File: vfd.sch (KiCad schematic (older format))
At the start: 28 parts, among them Q1 AO3400A, Q13 TO-252, Q14 CJT04N15, Q2 AO3400A, T1 Wuerth 760390013, T2 Wuerth 760390013, T3 Wuerth 760390013, U1 SN74AVC8T245PW, U4 MN12864K

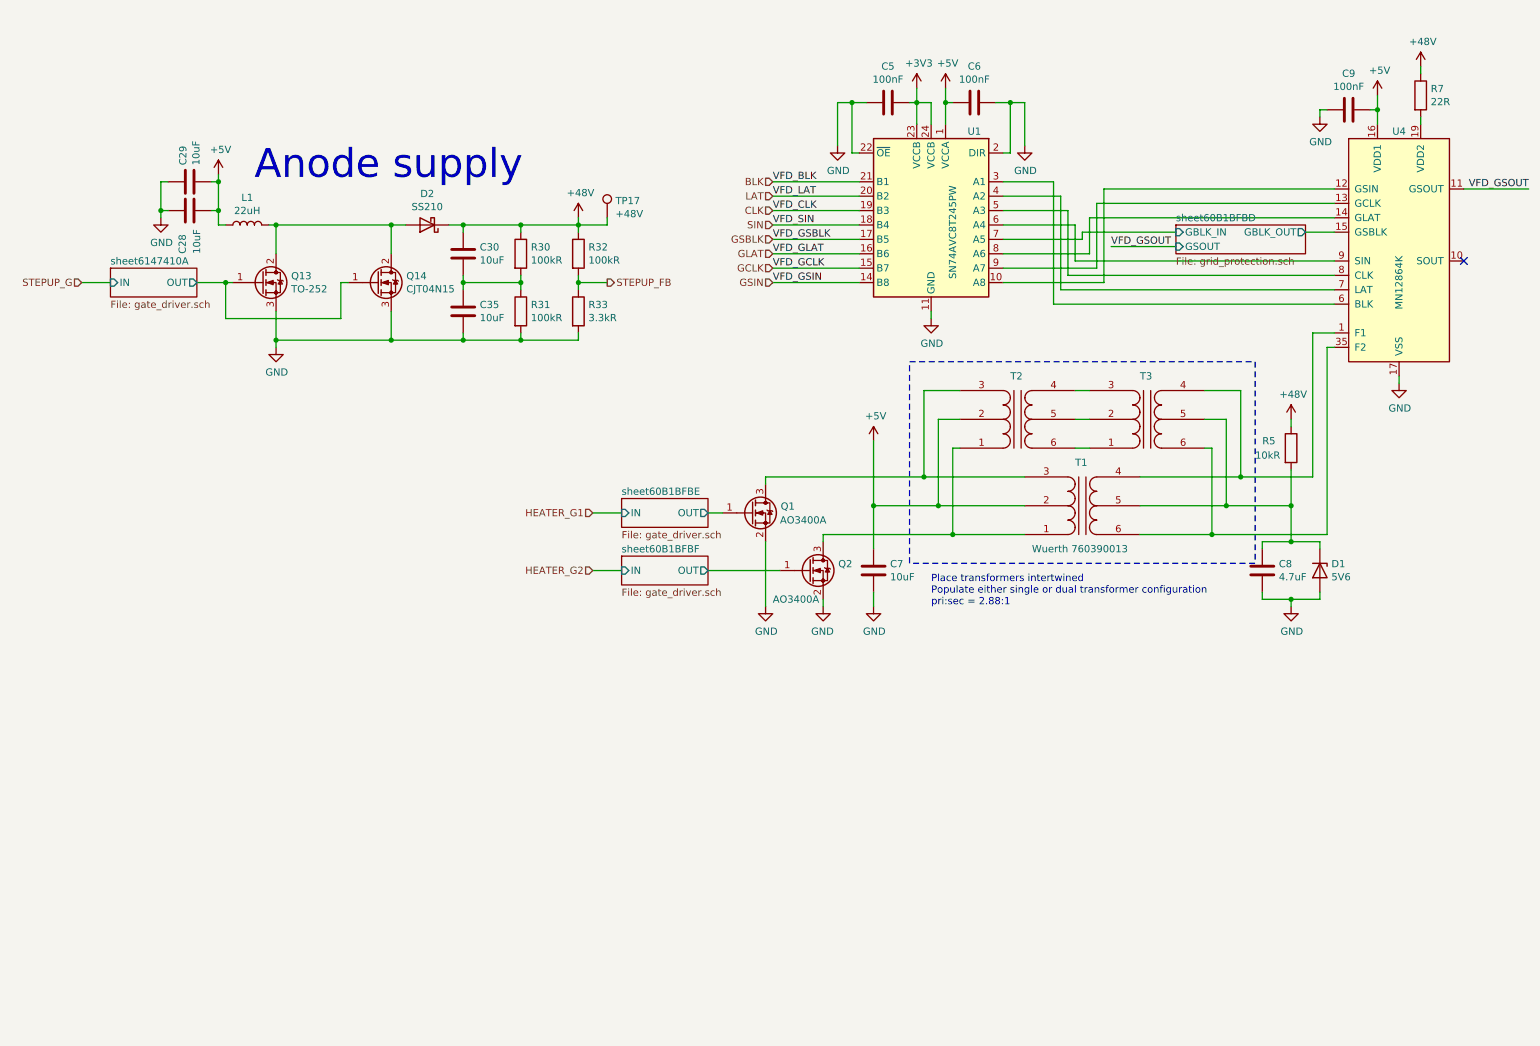
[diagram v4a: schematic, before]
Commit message: Add additional VFD VDD2 bulk capacitance
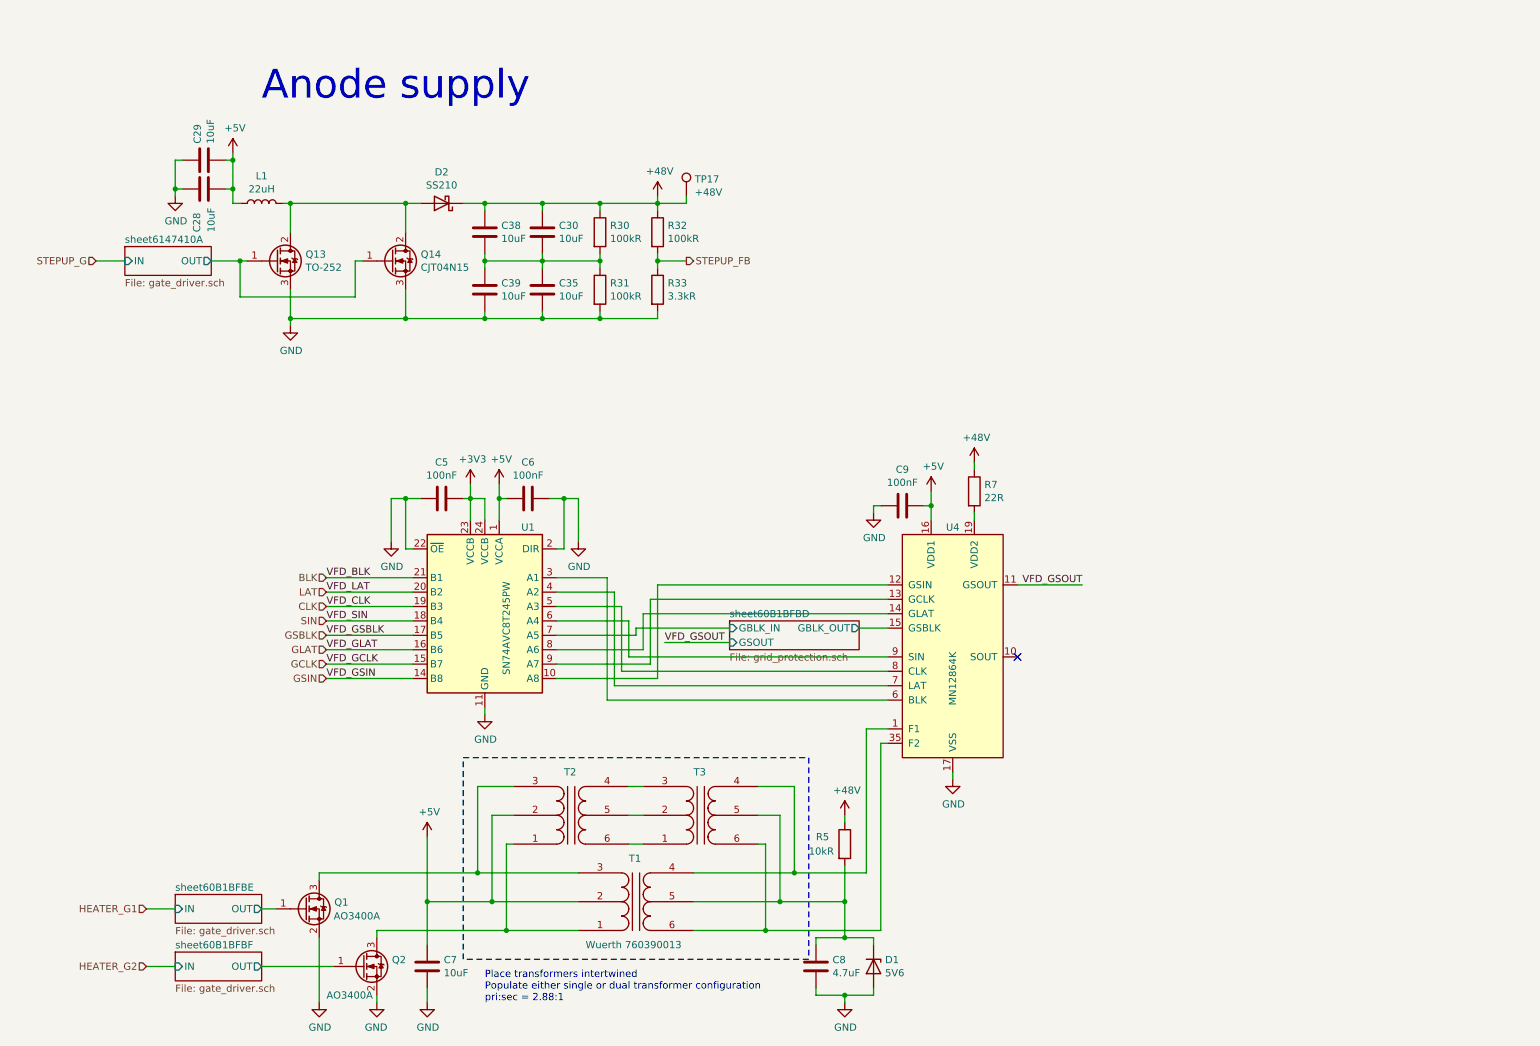
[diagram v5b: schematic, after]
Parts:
- added C38, C39: 10uF, Capacitor_SMD:C_1206_3216Metric, symbol Device:C
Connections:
- net +48V: now also C38.1
- net GND: now also C39.2
- net at C30.2, C35.1, R30.2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: now also C38.2, C39.1
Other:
- moved on the sheet: C28, C29, C30, C35, C5, C6, C7, C8, C9, D1, D2, L1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

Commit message: Add more VFD VDD2 bulk capacitance
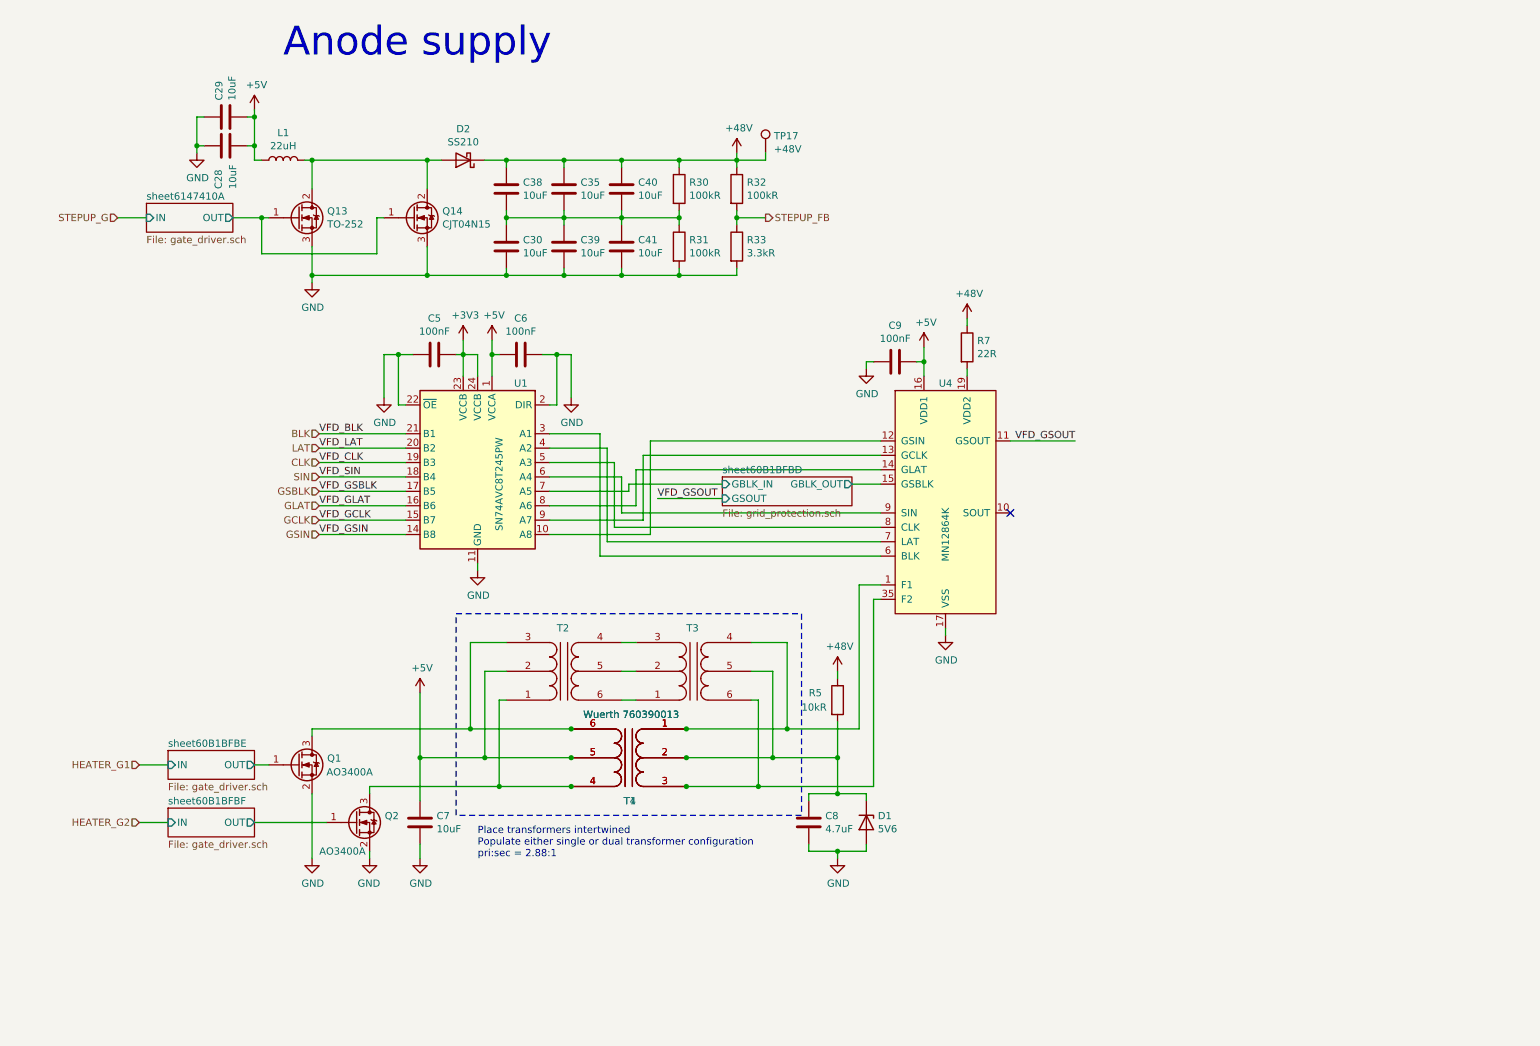
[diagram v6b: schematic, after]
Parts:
- added C40, C41: 10uF, Capacitor_SMD:C_0805_2012Metric, symbol Device:C
- added T4: Wuerth 760390013, Transformer_Würth:Transformer_Würth_12.60x8.30_6P, symbol Transformer_Isolation:Transformer_SP_SS
- C30, C35, C38, C39: footprint Capacitor_SMD:C_1206_3216Metric -> Capacitor_SMD:C_0805_2012Metric; LCSC C13585 -> C440198
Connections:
- net +48V: now also C35.1, C40.1; no longer C30.1
- net +5V: now also T1.5, T4.5; no longer T1.2
- net GND: now also C30.2, C41.2; no longer C35.2
- net at C38.2, C39.1, R30.2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: now also C30.1, C35.2, C40.2, C41.1; no longer C30.2, C35.1
- net at T3.4, U4.1 (F1), U4.2 (F1)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: now also T1.1, T4.1; no longer T1.4
- net at T3.6, U4.35 (F2), U4.36 (F1)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: now also T1.3, T4.3; no longer T1.6
- net at Q2.3 (D), T2.1: now also T1.4, T4.4; no longer T1.1
- net at Q1.3 (D), T2.3: now also T1.6, T4.6; no longer T1.3
- net at C8.1, D1.1 (K), R5.2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: now also T1.2, T4.2; no longer T1.5
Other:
- moved on the sheet: C28, C29, C38, C5, C6, C7, C8, C9, D1, D2, L1, Q1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

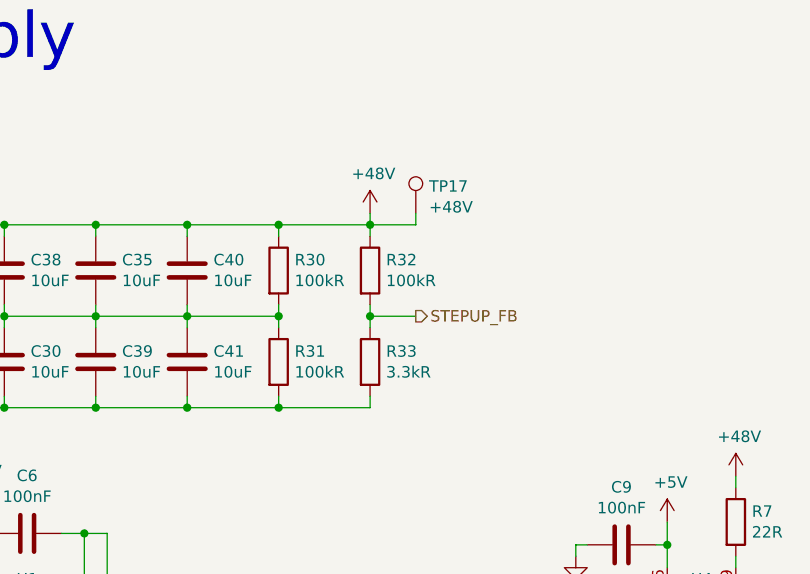
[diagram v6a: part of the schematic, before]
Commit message: Add more VFD VDD2 bypassing
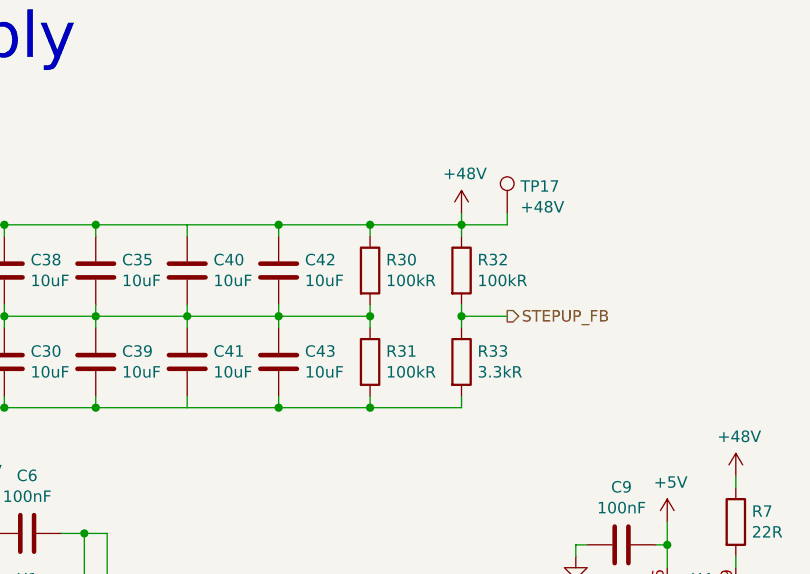
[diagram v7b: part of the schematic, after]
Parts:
- added C42, C43: 10uF, Capacitor_SMD:C_0805_2012Metric, symbol Device:C
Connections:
- net +48V: now also C42.1
- net GND: now also C43.2
- net at C30.1, C35.2, C38.2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: now also C42.2, C43.1
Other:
- moved on the sheet: R30, R31, R32, R33, TP17
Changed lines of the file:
@@
 L Device:R R?
 U 1 1 60D5616D
-P 5550 2150
+P 5950 2150
 AR Path="/60B03476/60D3C691/60D5616D" Ref="R?"  Part="1"
 AR Path="/60B03476/60D5616D" Ref="R33"  Part="1"
-F 0 "R33" H 5620 2196 50  0000 L CNN
-F 1 "3.3kR" H 5620 2105 50  0000 L CNN
-F 2 "Resistor_SMD:R_0402_1005Metric" V 5480 2150 50  0001 C CNN
-F 3 "https://datasheet.lcsc.com/szlcsc/Uniroyal-Elec-0402WGF5101TCE_C25905.pdf" H 5550 2150 50  0001 C CNN
-F 4 "C25890" H 5550 2150 50  0001 C CNN "LCSC"
-	1    5550 2150
+F 0 "R33" H 6020 2196 50  0000 L CNN
+F 1 "3.3kR" H 6020 2105 50  0000 L CNN
+F 2 "Resistor_SMD:R_0402_1005Metric" V 5880 2150 50  0001 C CNN
+F 3 "https://datasheet.lcsc.com/szlcsc/Uniroyal-Elec-0402WGF5101TCE_C25905.pdf" H 5950 2150 50  0001 C CNN
+F 4 "C25890" H 5950 2150 50  0001 C CNN "LCSC"
+	1    5950 2150
 	1    0    0    -1
 $EndComp
@@
 L Device:R R?
 U 1 1 60D56175
-P 5150 1750
+P 5550 1750
 AR Path="/60B03476/60D3C691/60D56175" Ref="R?"  Part="1"
 AR Path="/60B03476/60D56175" Ref="R30"  Part="1"
-F 0 "R30" H 5220 1796 50  0000 L CNN
-F 1 "100kR" H 5220 1705 50  0000 L CNN
-F 2 "Resistor_SMD:R_0805_2012Metric" V 5080 1750 50  0001 C CNN
-F 3 "https://datasheet.lcsc.com/szlcsc/Uniroyal-Elec-0805W8F1003T5E_C17407.pdf" H 5150 1750 50  0001 C CNN
-F 4 "C17407" H 5150 1750 50  0001 C CNN "LCSC"
-	1    5150 1750
+F 0 "R30" H 5620 1796 50  0000 L CNN
+F 1 "100kR" H 5620 1705 50  0000 L CNN
+F 2 "Resistor_SMD:R_0805_2012Metric" V 5480 1750 50  0001 C CNN
+F 3 "https://datasheet.lcsc.com/szlcsc/Uniroyal-Elec-0805W8F1003T5E_C17407.pdf" H 5550 1750 50  0001 C CNN
+F 4 "C17407" H 5550 1750 50  0001 C CNN "LCSC"
+	1    5550 1750
 	1    0    0    -1
 $EndComp
@@
 L Device:R R?
 U 1 1 60D5617C
-P 5150 2150
+P 5550 2150
 AR Path="/60B03476/60D3C691/60D5617C" Ref="R?"  Part="1"
 AR Path="/60B03476/60D5617C" Ref="R31"  Part="1"
-F 0 "R31" H 5220 2196 50  0000 L CNN
-F 1 "100kR" H 5220 2105 50  0000 L CNN
-F 2 "Resistor_SMD:R_0805_2012Metric" V 5080 2150 50  0001 C CNN
-F 3 "https://datasheet.lcsc.com/szlcsc/Uniroyal-Elec-0805W8F1003T5E_C17407.pdf" H 5150 2150 50  0001 C CNN
-F 4 "C17407" H 5150 2150 50  0001 C CNN "LCSC"
-	1    5150 2150
+F 0 "R31" H 5620 2196 50  0000 L CNN
+F 1 "100kR" H 5620 2105 50  0000 L CNN
+F 2 "Resistor_SMD:R_0805_2012Metric" V 5480 2150 50  0001 C CNN
+F 3 "https://datasheet.lcsc.com/szlcsc/Uniroyal-Elec-0805W8F1003T5E_C17407.pdf" H 5550 2150 50  0001 C CNN
+F 4 "C17407" H 5550 2150 50  0001 C CNN "LCSC"
+	1    5550 2150
 	1    0    0    -1
 $EndComp
@@
 L power:+48V #PWR?
 U 1 1 60D5619B
-P 5550 1500
+P 5950 1500
 AR Path="/60B03476/60D3C691/60D5619B" Ref="#PWR?"  Part="1"
 AR Path="/60B03476/60D5619B" Ref="#PWR0163"  Part="1"
-F 0 "#PWR0163" H 5550 1350 50  0001 C CNN
-F 1 "+48V" H 5565 1673 50  0000 C CNN
-F 2 "" H 5550 1500 50  0001 C CNN
-F 3 "" H 5550 1500 50  0001 C CNN
-	1    5550 1500
-	1    0    0    -1
-$EndComp
-Wire Wire Line
-	5550 1500 5550 1550
-Connection ~ 5550 1550
+F 0 "#PWR0163" H 5950 1350 50  0001 C CNN
+F 1 "+48V" H 5965 1673 50  0000 C CNN
+F 2 "" H 5950 1500 50  0001 C CNN
+F 3 "" H 5950 1500 50  0001 C CNN
+	1    5950 1500
+	1    0    0    -1
+$EndComp
+Wire Wire Line
+	5950 1500 5950 1550
+Connection ~ 5950 1550
 $Comp
 L Connector:TestPoint TP?
 U 1 1 60D561B2
-P 5750 1500
+P 6150 1500
 AR Path="/60B03476/60D3C691/60D561B2" Ref="TP?"  Part="1"
 AR Path="/60B03476/60D561B2" Ref="TP17"  Part="1"
-F 0 "TP17" H 5808 1618 50  0000 L CNN
-F 1 "+48V" H 5808 1527 50  0000 L CNN
-F 2 "TestPoint:TestPoint_Pad_2.0x2.0mm" H 5950 1500 50  0001 C CNN
-F 3 "~" H 5950 1500 50  0001 C CNN
-	1    5750 1500
-	1    0    0    -1
-$EndComp
-Wire Wire Line
-	5750 1500 5750 1550
-Wire Wire Line
-	5750 1550 5550 1550
+F 0 "TP17" H 6208 1618 50  0000 L CNN
+F 1 "+48V" H 6208 1527 50  0000 L CNN
+F 2 "TestPoint:TestPoint_Pad_2.0x2.0mm" H 6350 1500 50  0001 C CNN
+F 3 "~" H 6350 1500 50  0001 C CNN
+	1    6150 1500
+	1    0    0    -1
+$EndComp
+Wire Wire Line
+	6150 1500 6150 1550
+Wire Wire Line
+	6150 1550 5950 1550
 $Comp
 L Transformer_Isolation:Transformer_SP_SS T?
@@
 Connection ~ 2250 1950
 Wire Wire Line
-	5550 1900 5550 1950
+	5950 1900 5950 1950
 $Comp
 L Device:R R?
 U 1 1 614B31AF
-P 5550 1750
+P 5950 1750
 AR Path="/60B03476/60D3C691/614B31AF" Ref="R?"  Part="1"
 AR Path="/60B03476/614B31AF" Ref="R32"  Part="1"
-F 0 "R32" H 5620 1796 50  0000 L CNN
-F 1 "100kR" H 5620 1705 50  0000 L CNN
-F 2 "Resistor_SMD:R_0805_2012Metric" V 5480 1750 50  0001 C CNN
-F 3 "https://datasheet.lcsc.com/szlcsc/Uniroyal-Elec-0805W8F1003T5E_C17407.pdf" H 5550 1750 50  0001 C CNN
-F 4 "C17407" H 5550 1750 50  0001 C CNN "LCSC"
-	1    5550 1750
-	1    0    0    -1
-$EndComp
-Text HLabel 5750 1950 2    50   Output ~ 0
+F 0 "R32" H 6020 1796 50  0000 L CNN
+F 1 "100kR" H 6020 1705 50  0000 L CNN
+F 2 "Resistor_SMD:R_0805_2012Metric" V 5880 1750 50  0001 C CNN
+F 3 "https://datasheet.lcsc.com/szlcsc/Uniroyal-Elec-0805W8F1003T5E_C17407.pdf" H 5950 1750 50  0001 C CNN
+F 4 "C17407" H 5950 1750 50  0001 C CNN "LCSC"
+	1    5950 1750
+	1    0    0    -1
+$EndComp
+Text HLabel 6150 1950 2    50   Output ~ 0
 STEPUP_FB
 Wire Wire Line
-	5750 1950 5550 1950
-Connection ~ 5550 1950
-Wire Wire Line
-	5550 1950 5550 2000
+	6150 1950 5950 1950
+Connection ~ 5950 1950
+Wire Wire Line
+	5950 1950 5950 2000
 Wire Wire Line
 	2600 1550 3400 1550
 Wire Wire Line
+	5950 1600 5950 1550
+Wire Wire Line
 	5550 1600 5550 1550
-Wire Wire Line
-	5150 1600 5150 1550
 Wire Wire Line
 	4350 1600 4350 1550
@@
 	2250 2200 2250 1950
 Wire Wire Line
-	5550 2300 5550 2350
+	5950 2300 5950 2350
 Wire Wire Line
 	3400 2150 3400 2350
@@
 	4350 2300 4350 2350
 Wire Wire Line
-	5150 2350 5150 2300
+	5550 2350 5550 2300
 Wire Wire Line
 	2600 2150 2600 2350
@@
 	2600 2350 2600 2400
 Wire Wire Line
-	5550 1550 5150 1550
-Wire Wire Line
-	5550 2350 5150 2350
+	5950 1550 5550 1550
+Wire Wire Line
+	5950 2350 5550 2350
 Wire Wire Line
 	6500 4600 6500 5900
@@
 	4750 5300 4850 5300
 Wire Wire Line
+	5550 1900 5550 1950
+Wire Wire Line
+	5550 1550 5150 1550
+Connection ~ 5550 1550
+Wire Wire Line
+	5150 1950 5550 1950
+Connection ~ 5550 1950
+Wire Wire Line
+	5550 1950 5550 2000
+Wire Wire Line
+	5550 2350 5150 2350
+Connection ~ 5550 2350
+$Comp
+L Device:C C?
+U 1 1 602BFA35
+P 5150 1750
+AR Path="/60B03476/60D3C691/602BFA35" Ref="C?"  Part="1"
+AR Path="/60B03476/602BFA35" Ref="C42"  Part="1"
+F 0 "C42" H 5265 1796 50  0000 L CNN
+F 1 "10uF" H 5265 1705 50  0000 L CNN
+F 2 "Capacitor_SMD:C_0805_2012Metric" H 5188 1600 50  0001 C CNN
+F 3 "https://datasheet.lcsc.com/szlcsc/Samsung-Electro-Mechanics-CL31A106KBHNNNE_C13585.pdf" H 5150 1750 50  0001 C CNN
+F 4 "C440198" H 5150 1750 50  0001 C CNN "LCSC"
+	1    5150 1750
+	1    0    0    -1
+$EndComp
+Wire Wire Line
 	5150 1900 5150 1950
-Wire Wire Line
-	5150 1550 4750 1550
+Connection ~ 5150 1950
+Wire Wire Line
+	5150 1950 5150 2000
+Wire Wire Line
+	5150 1600 5150 1550
+Wire Wire Line
+	5150 2300 5150 2350
+$Comp
+L Device:C C?
+U 1 1 602BFA41
+P 5150 2150
+AR Path="/60B03476/60D3C691/602BFA41" Ref="C?"  Part="1"
+AR Path="/60B03476/602BFA41" Ref="C43"  Part="1"
+F 0 "C43" H 5265 2196 50  0000 L CNN
+F 1 "10uF" H 5265 2105 50  0000 L CNN
+F 2 "Capacitor_SMD:C_0805_2012Metric" H 5188 2000 50  0001 C CNN
+F 3 "https://datasheet.lcsc.com/szlcsc/Samsung-Electro-Mechanics-CL31A106KBHNNNE_C13585.pdf" H 5150 2150 50  0001 C CNN
+F 4 "C440198" H 5150 2150 50  0001 C CNN "LCSC"
+	1    5150 2150
+	1    0    0    -1
+$EndComp
+Wire Wire Line
+	4750 1550 5150 1550
+Wire Wire Line
+	5150 2350 4750 2350
+Wire Wire Line
+	4750 1950 5150 1950
 Connection ~ 5150 1550
-Connection ~ 4750 1550
-Wire Wire Line
-	4750 1950 5150 1950
-Connection ~ 5150 1950
-Wire Wire Line
-	5150 1950 5150 2000
-Wire Wire Line
-	5150 2350 4750 2350
 Connection ~ 5150 2350
-Connection ~ 4750 2350
 $EndSCHEMATC
